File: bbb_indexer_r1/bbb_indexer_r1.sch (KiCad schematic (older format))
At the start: 29 parts, among them P8 BeagleBone_Black_Header_P8, P9 BeagleBone_Black_Header_P9

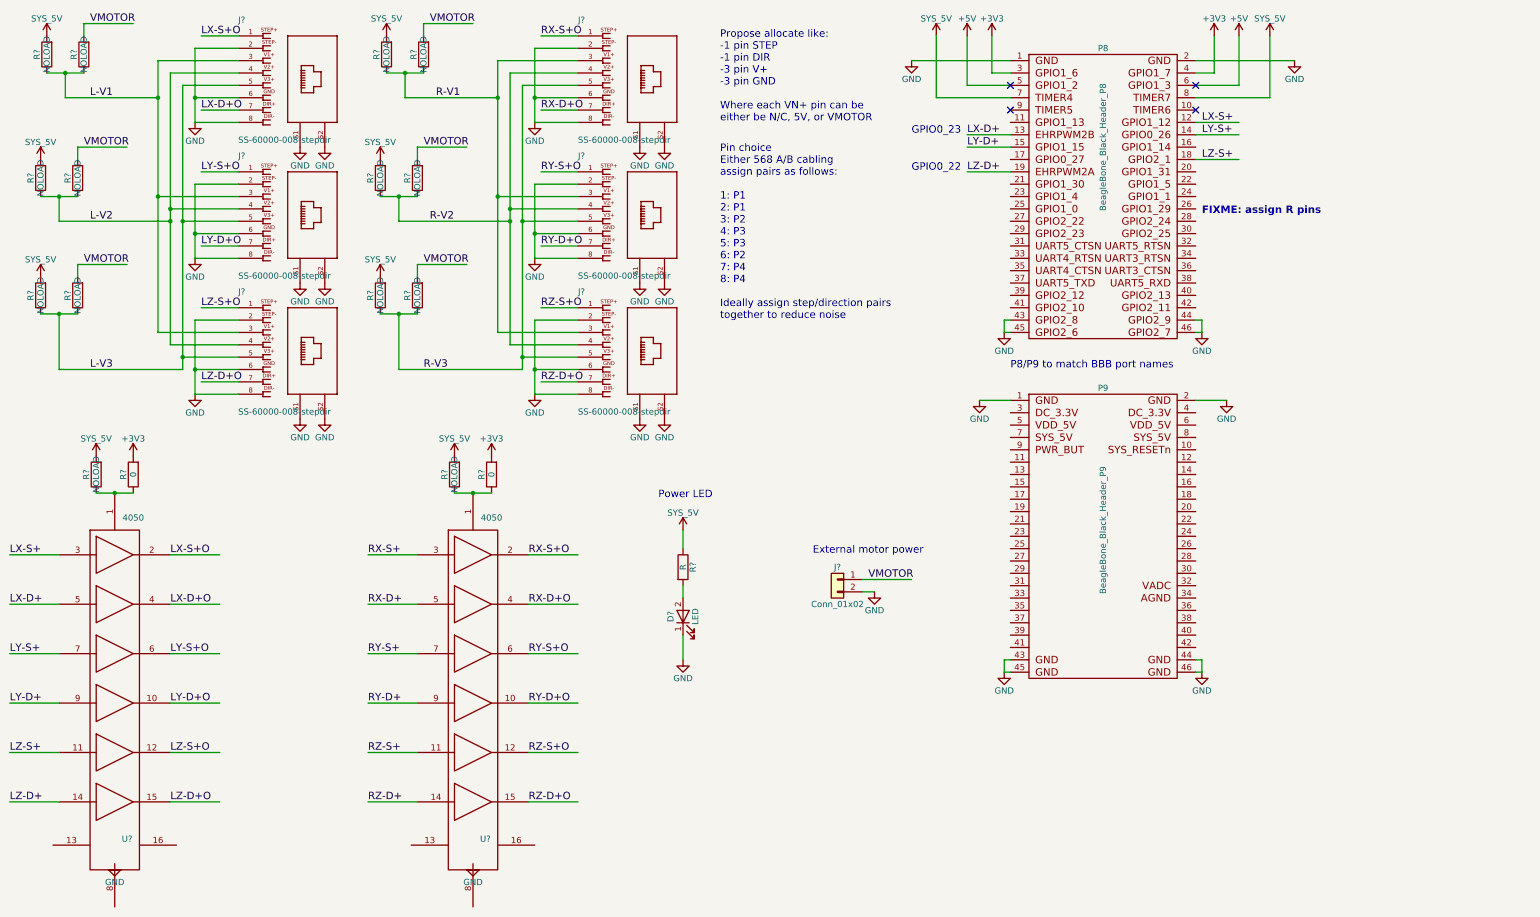
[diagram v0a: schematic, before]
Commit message: Design using GPIO much more exhaustively
Signed-off-by: John McMaster <johndmcmaster@gmail.com>
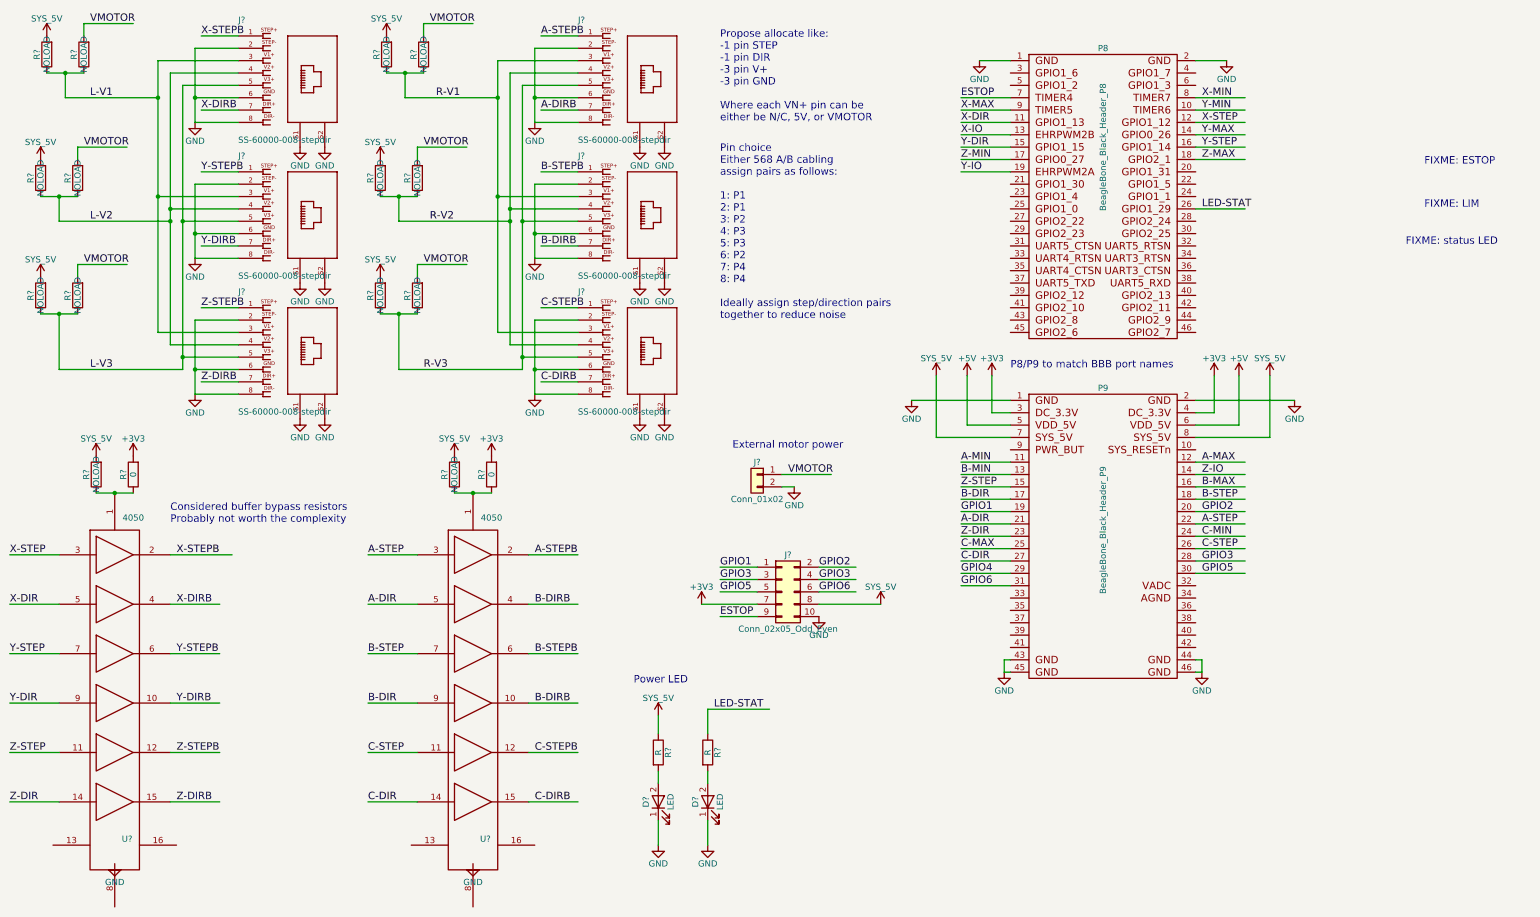
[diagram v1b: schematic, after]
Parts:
- added D?: LED, symbol LED
- added J?: Conn_02x05_Odd_Even, symbol Conn_02x05_Odd_Even
- added R?: R, symbol R
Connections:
- net labels added: A-DIR, A-DIRB, A-MAX, A-MIN, A-STEP, A-STEPB, B-DIR, B-DIRB, B-MAX, B-MIN, B-STEP, B-STEPB, C-DIR, C-DIRB, C-MAX, C-MIN, C-STEP, C-STEPB, ESTOP, GPIO1, GPIO2, GPIO3, GPIO4, GPIO5, GPIO6, LED-STAT, X-DIR, X-DIRB, X-IO, X-MAX, X-MIN, X-STEP, X-STEPB, Y-DIR, Y-DIRB, Y-IO, Y-MAX, Y-MIN, Y-STEP, Y-STEPB, Z-DIR, Z-DIRB, Z-IO, Z-MAX, Z-MIN, Z-STEP, Z-STEPB
- net labels removed: LX-D+, LX-D+O, LX-S+, LX-S+O, LY-D+, LY-D+O, LY-S+, LY-S+O, LZ-D+, LZ-D+O, LZ-S+, LZ-S+O, RX-D+, RX-D+O, RX-S+, RX-S+O, RY-D+, RY-D+O, RY-S+, RY-S+O, RZ-D+, RZ-D+O, RZ-S+, RZ-S+O
- wire segments 157 -> 219
- no-connect marks 4 -> 0
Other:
- note added: "Considered buffer bypass resistors\nProbably not worth the complexity"
- note added: "FIXME: ESTOP"
- note added: "FIXME: LIM"
- note added: "FIXME: status LED"
- note removed: "FIXME: assign R pins"
- note removed: "GPIO0_22"
- note removed: "GPIO0_23"
- moved on the sheet: D?, J?, R?

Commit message: Schematic RC complete
Signed-off-by: John McMaster <johndmcmaster@gmail.com>
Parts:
- removed J? (x3): SS-60000-008-stepdir, 520260-4, symbol SS-60000-008-stepdir
- removed R? (x12): NOLOAD, symbol R
- added J4, J5, J6: SS-60000-008-stepdir, 520260-4, symbol SS-60000-008-stepdir
- added R1, R10, R11, R12, R15, R16, R17, R18, R19, R2, R21, R22, R24, R25, R3, R4, R5, R6, R7, R8, R9: Pad3, symbol Pad3
- gave numbers to parts that had none: 15
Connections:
- net labels removed: +5V
- wire segments 219 -> 220
- no-connect marks 0 -> 45
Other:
- note added: "P8/P9 to match BBB connector names"
- note added: "Pad3 => 3 SMD resistor pads\nCan be placed on either or none"
- note added: "TODO: consider using multiple sheets"
- note removed: "Considered buffer bypass resistors\nProbably not worth the complexity"
- note removed: "FIXME: ESTOP"
- note removed: "FIXME: LIM"
- note removed: "FIXME: status LED"
- note removed: "P8/P9 to match BBB port names"
- moved on the sheet: D1, D2, J1, J2, J3, J7, J8, P8, P9, R13, R14, R27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

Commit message: routing mostly complete
Signed-off-by: John McMaster <johndmcmaster@gmail.com>
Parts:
- removed R13, R27: NOLOAD, symbol R
- removed R14, R28: 0, symbol R
- added R13, R14: Pad3, lib:R3_0603, symbol Pad3
- D1, D2: footprint (none) -> LEDs:LED_0603
- J1, J2, J3, J4, J5, J6: footprint 520260-4 -> SS-60000-008:520260-4
- J7: footprint (none) -> Pin_Headers:Pin_Header_Straight_1x02_Pitch2.54mm
- J8: footprint (none) -> Pin_Headers:Pin_Header_Straight_2x05_Pitch2.54mm
- P8, P9: footprint (none) -> lib:Socket_BeagleBone_Black
- R1, R10, R11, R12, R15, R16, R17, R18, R19, R2, R21, R22, R24, R25, R3, R4, R5, R6, R7, R8, R9: footprint (none) -> lib:R3_0603
- R29, R30: footprint (none) -> Resistors_SMD:R_0603
- U1, U2: footprint (none) -> Housings_SOIC:SOIC-16_3.9x9.9mm_Pitch1.27mm
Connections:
- net labels added: L-VREF, R-VREF
- wire segments 220 -> 228
- no-connect marks 45 -> 49
